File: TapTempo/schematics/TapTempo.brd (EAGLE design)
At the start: 60.6 x 50.5 mm, 40 parts, among them IC1 TL072D, IC2 MEGA168, IC3 LT1257S, Q301 BC846, Q701 BC846, Y1 16Mhz

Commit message: preliminary routing
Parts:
- removed C4: 100n, resistor:C0603
- removed IC3: LT1257S, linear-technology:SOIC8
- removed R2: 51K, resistor:R0603
- added BUTTON: (no value), SparkFun:1X04
- added C201: 100n, resistor:C0603
- added IC4: LM4041A12DBZ, texas:DBZ_R-PDSO-G3
- added R201: 100R, resistor:R0603
- added R202: 5K, resistor:R0603
- added R401, R402, R403, R404: 1K, resistor:R0603
- added U$1: MCP4921, Rebel:SOIC8
- moved IC1 32.7 mm to (36.2, 35.6), turned to 90 degrees
- moved R303 27.0 mm to (38.1, 19.7), turned to 270 degrees
- moved R301 22.2 mm to (36.8, 12.1), turned to 90 degrees
- moved R302 20.5 mm to (39.4, 12.1), turned to 90 degrees
- moved C3 20.4 mm to (14.6, 25.4), turned to 270 degrees
- moved Q301 18.9 mm to (38.1, 16.5), turned to 0 degrees
- moved R104 11.4 mm to (43.8, 19.1), turned to 180 degrees
- moved C1 9.55 mm to (24.8, 8.89), turned to 0 degrees
- moved R105 9.16 mm to (49.5, 27.9), turned to 0 degrees
- moved D2 8.89 mm to (12.1, 45.1)
- moved F2 8.26 mm to (20.3, 45.1)
- moved R101 7.18 mm to (49.5, 25.4)
- moved R102 7.18 mm to (49.5, 22.9), turned to 180 degrees
- moved R103 7.18 mm to (49.5, 30.5), turned to 0 degrees
- moved R1 5.85 mm to (28.6, 8.89), turned to 0 degrees
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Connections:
- removed net N$43: U$2.13, U$2.14
- removed net PWR_BUS: U$2.15, U$2.16
- removed net VCC: IC2.6
- new net LED+: BUTTON.3
- new net LED-: BUTTON.4
- new net N$13: R201.2, U$1.8
- new net N$19: IC1.6, R401.2, R403.1
- new net RAMP: IC1.5, R201.1, R402.1
- new net S1: BUTTON.1
- new net S2: BUTTON.2
- new net VREF: IC4.1, R202.2, R401.1, U$1.6
- net +12V: now also R202.1
- net +5V: now also C201.1, IC2.6, U$1.1; no longer C4.1, IC3.8
- net GND: now also C201.2, IC4.2, R402.2, U$1.7; no longer C4.2, IC3.5
- net N$7: now also R403.2, R404.1; no longer R2.1
- net N$8: now also R404.2; no longer R2.2
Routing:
- net +5V: track 0.00 -> 117.4 mm, vias 0 -> 2
- net +12V: track 0.00 -> 80.0 mm, vias 0 -> 2
- net N$1: track 0.00 -> 64.6 mm, vias 0 -> 1
- net GND: track 0.00 -> 63.2 mm, vias 0 -> 8
- net -12V: track 0.00 -> 46.8 mm
- net N$28: track 0.00 -> 38.6 mm, vias 0 -> 2
- net CMBOUT: track 0.00 -> 36.5 mm, vias 0 -> 2
- net VREF: track 0.00 -> 32.3 mm
- net DIVIN: track 0.00 -> 30.8 mm
- net RAMP: track 0.00 -> 29.9 mm
- net RX: track 0.00 -> 25.1 mm, vias 0 -> 1
- net N$3: track 0.00 -> 25.0 mm, vias 0 -> 2
- net N$2: track 0.00 -> 24.3 mm
- net TX: track 0.00 -> 24.1 mm, vias 0 -> 1
- net MODEA: track 0.00 -> 23.8 mm
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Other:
- board text added: "Rev 01"
- board text added: "Tap Tempo"
- board text removed: "Clock Delay"
- board text removed: "Rev 02"

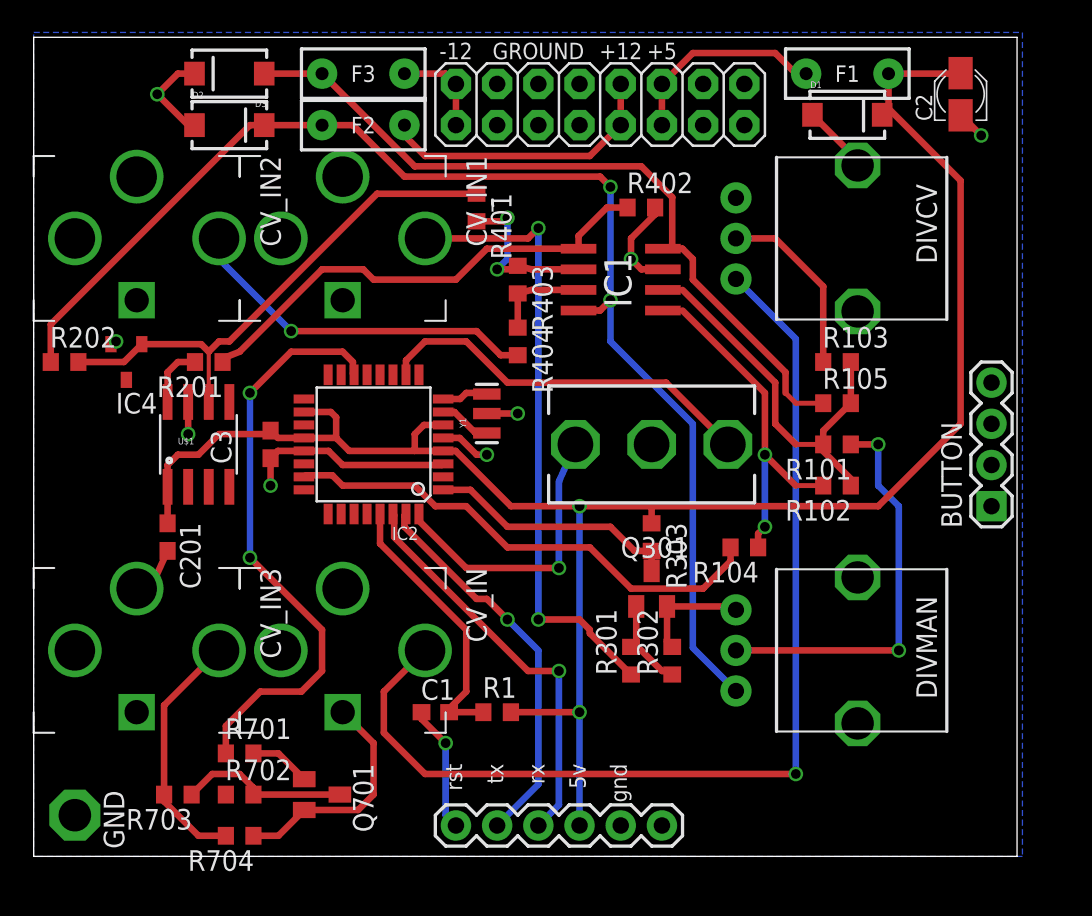
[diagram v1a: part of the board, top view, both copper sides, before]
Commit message: routed board with offsetting op amp as per MCP4921 datasheet
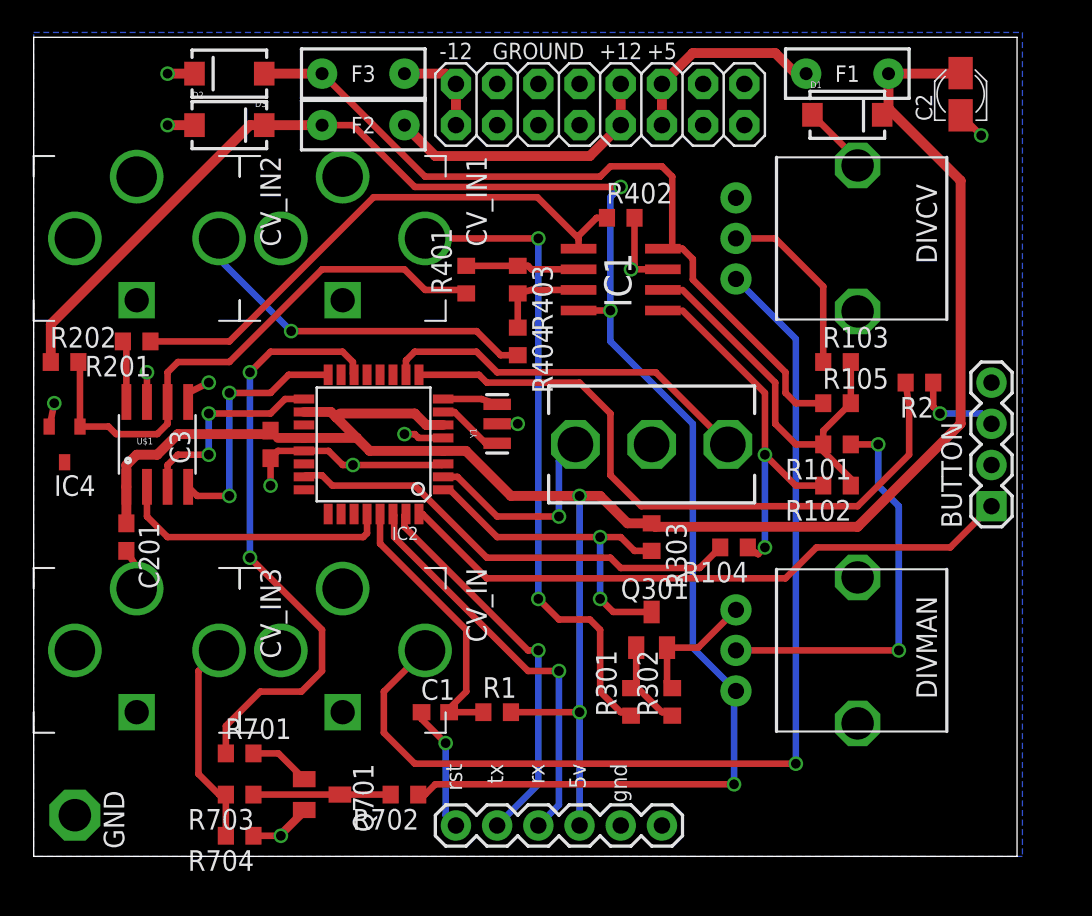
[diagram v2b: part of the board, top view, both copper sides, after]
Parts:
- added R2: 10K, resistor:R0603
- R403: value 1K -> 51K
- moved R702 10.2 mm to (22.9, 3.81), turned to 180 degrees
- moved IC4 6.35 mm to (1.91, 25.4)
- moved R201 4.62 mm to (6.35, 31.8)
- moved R401 4.49 mm to (26.7, 35.6), turned to 90 degrees
- moved R703 3.81 mm to (12.7, 3.81)
- moved C201 2.54 mm to (5.71, 19.7)
- moved Q301 2.54 mm to (38.1, 14.0)
- moved U$1 2.54 mm to (7.62, 25.4)
- moved R301 2.54 mm to (36.8, 9.53)
- moved R302 2.54 mm to (39.4, 9.53)
- moved R402 1.42 mm to (36.2, 39.4)
- moved Y1 0.90 mm to (28.6, 26.7)
- moved R104 0.63 mm to (43.2, 19.1)
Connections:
- net CLKIN renamed TRIGIN
- net CMBOUT renamed CLKOUT
- net DIVIN renamed SPEEDIN
- net MODEA renamed MODESW
- removed net LED-: BUTTON.4
- removed net N$17: IC2.28
- removed net RSTIN: IC2.32, S1.3
- removed net S1: BUTTON.1
- removed net S2: BUTTON.2
- removed net TRIGA: IC2.2
- new net CS: IC2.28, U$1.2
- new net SCK: IC2.17, U$1.3
- new net SDI: IC2.16, U$1.4
- new net STOPSW: IC2.2, S1.3
- new net SW1: BUTTON.1, IC2.32
- net +12V: now also R702.1
- net ALTA: now also R2.2
- net GND: now also BUTTON.2, BUTTON.4, U$1.5
- net LED+: now also R2.1
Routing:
- net ALTA: track 0.00 -> 41.6 mm
- net SW1: track 0.00 -> 38.8 mm
- net +12V: track 80.0 -> 106.2 mm, vias 2 -> 3
- net RSTIN: track 18.1 -> 0.00 mm, vias 1 -> 0
- net CS: track 0.00 -> 17.2 mm
- net SDI: track 0.00 -> 15.7 mm, vias 0 -> 2
- net STOPSW: track 0.00 -> 13.0 mm, vias 0 -> 1
- net SCK: track 0.00 -> 12.9 mm, vias 0 -> 2
- net GND: track 63.2 -> 54.3 mm, vias 8 -> 12
- net +5V: track 117.4 -> 125.1 mm
- net TRIGIN: track 15.6 -> 21.7 mm, vias 0 -> 2
- net LED+: track 0.00 -> 5.52 mm, vias 0 -> 1
- net RAMP: track 29.9 -> 34.1 mm
- net N$9: track 10.6 -> 7.01 mm, vias 2 -> 0
- net N$35: track 15.4 -> 12.9 mm
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
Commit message: updated routing
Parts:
- removed R201: 100R, resistor:R0603
- removed R404: 1K, resistor:R0603
- R202: value 5K -> 1K
- R401, R402: value 1K -> 120k
- R403: value 51K -> 100R
- moved R402 7.41 mm to (29.8, 35.6), turned to 270 degrees
- moved R703 4.02 mm to (8.89, 5.08)
- moved R704 4.02 mm to (8.89, 2.54)
- moved R403 3.81 mm to (29.8, 31.8)
- moved C201 3.59 mm to (3.17, 22.2), turned to 180 degrees
- moved C1 3.42 mm to (27.9, 10.2), turned to 180 degrees
- moved R1 1.42 mm to (27.9, 7.62)
- moved R702 1.27 mm to (22.9, 5.08)
- moved IC4 1.27 mm to (3.17, 25.4)
- moved R202 1.27 mm to (3.17, 30.5)
- moved R2 1.27 mm to (54.6, 30.5)
- moved R701 1.27 mm to (12.7, 5.08)
- moved R401 0.63 mm to (27.3, 35.6), turned to 270 degrees
- turned GND to 0 degrees
- renumbered CV_IN to SPEED, CV_IN1 to TRIG, CV_IN2 to RAMP, CV_IN3 to CLK, DIVCV to CV, DIVMAN to MANUAL
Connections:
- removed net N$13: R201.2, U$1.8
- net GND: now also R401.2, RAMP.P$1, RAMP.P$2, TRIG.P$4; no longer R402.2
- net N$7: now also R402.2, R403.1; no longer R403.2, R404.1
- net N$8: now also R403.2; no longer R404.2
- net N$9: now also R401.1, R402.1; no longer R401.2, R403.1
- net RAMP: now also U$1.8; no longer R201.1, R402.1
- net VREF: no longer R401.1
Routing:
- net VREF: track 34.7 -> 9.95 mm
- net GND: track 54.3 -> 43.8 mm, vias 12 -> 16
- net N$38: track 8.46 -> 13.4 mm
- net N$13: track 3.82 -> 0.00 mm
- net N$1: track 63.7 -> 60.1 mm
- net N$29: track 7.86 -> 11.3 mm
- net -12V: track 48.1 -> 45.1 mm
- net +12V: track 106.2 -> 103.5 mm, vias 3 -> 2
- net RAMP: track 34.1 -> 36.6 mm
- net +5V: track 125.1 -> 126.6 mm
- net N$35: track 12.9 -> 11.6 mm
- net LED+: track 5.52 -> 6.79 mm
- net ALTA: track 41.6 -> 42.8 mm
- net RX: track 25.1 -> 24.0 mm
- net N$39: track 17.0 -> 15.9 mm
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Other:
- board size 60.6 x 50.5 mm -> 60.6 x 50.3 mm

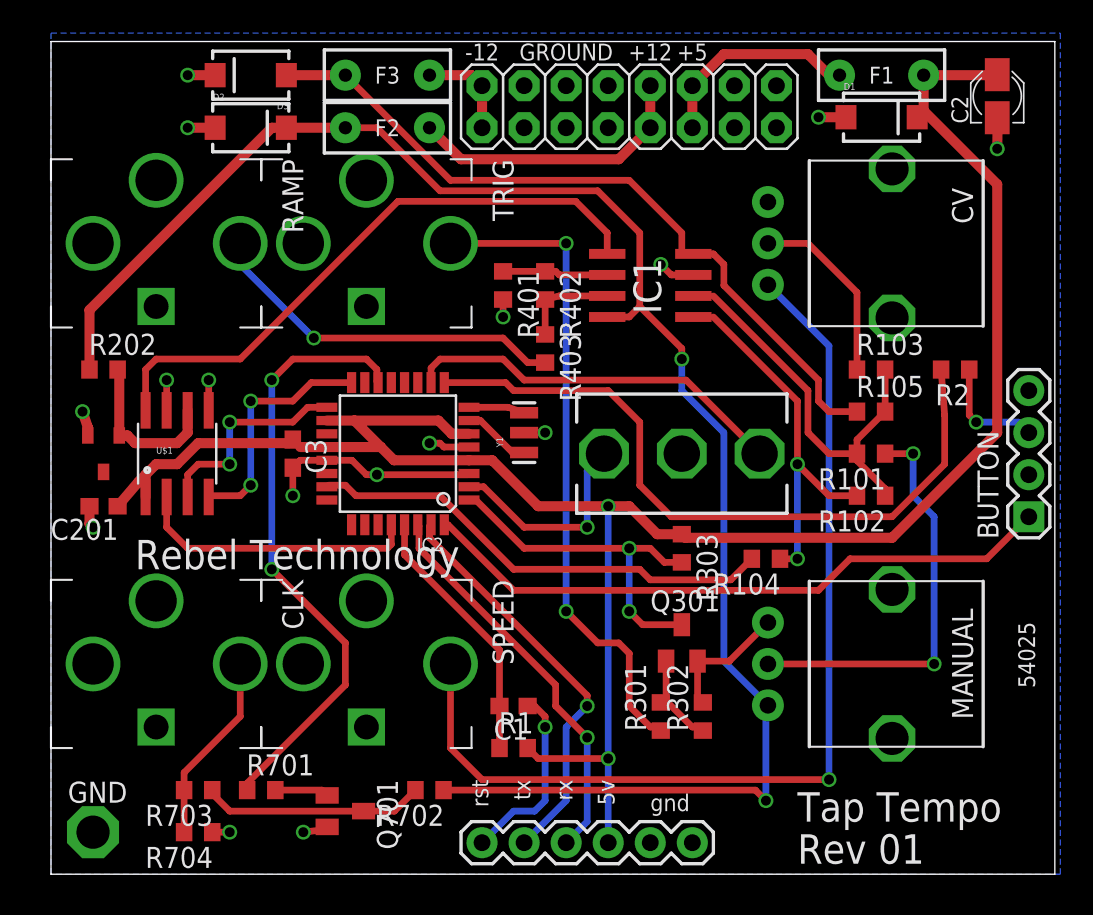
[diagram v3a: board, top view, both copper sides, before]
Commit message: re-aligned labels
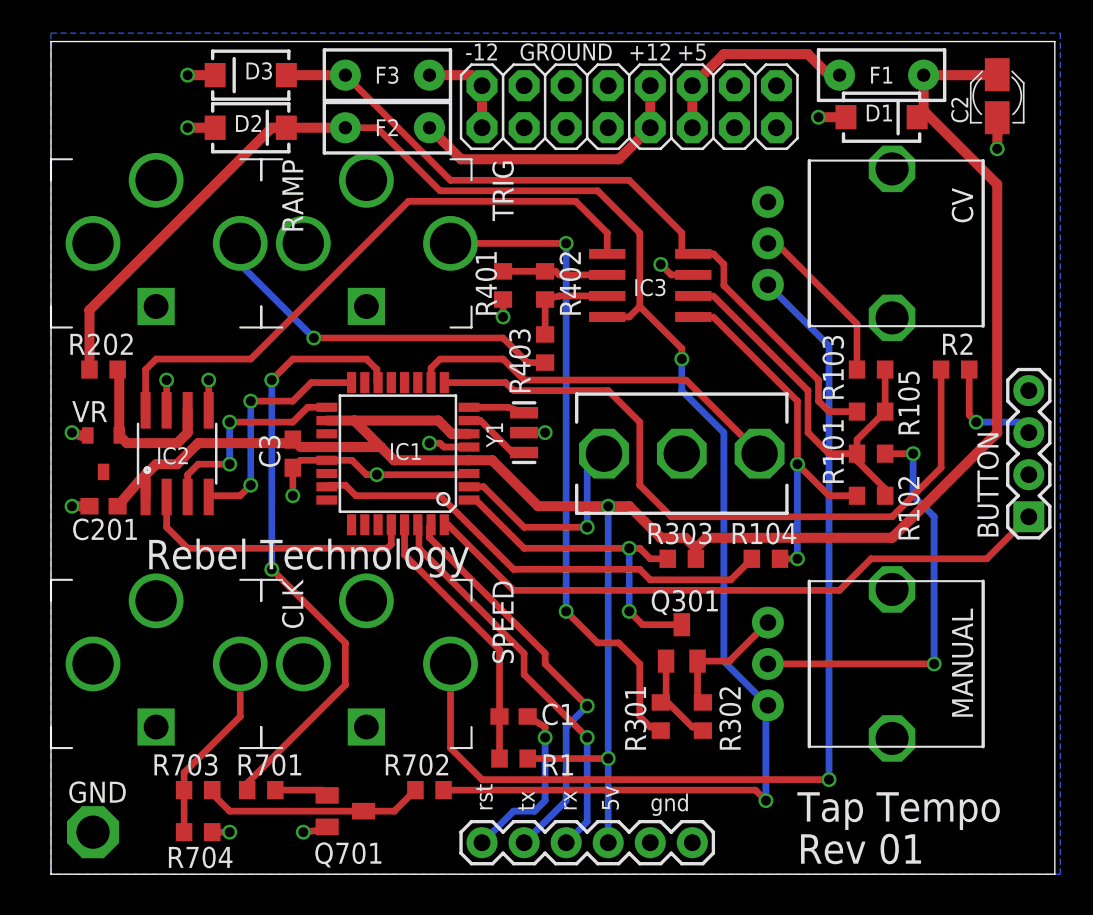
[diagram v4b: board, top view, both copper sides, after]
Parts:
- removed U$1: MCP4921, Rebel:SOIC8
- added IC3: TL072D, linear:SO08
- IC1: value TL072D -> MEGA168; device linear:SO08 -> atmel:TQFP32-08
- IC2: value MEGA168 -> MCP4921; device atmel:TQFP32-08 -> Rebel:SOIC8
- moved IC1 18.3 mm to (21.0, 25.4), turned to 180 degrees
- moved IC2 13.3 mm to (7.62, 25.4), turned to 0 degrees
- moved C1 0.63 mm to (27.9, 9.53)
- moved R1 0.63 mm to (27.9, 6.99)
- moved R303 0.63 mm to (38.1, 19.1), turned to 180 degrees
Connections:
- net +12V: now also IC3.8; no longer IC1.8
- net +5V: now also IC1.18, IC1.20, IC1.4, IC1.6, IC2.1; no longer IC2.18, IC2.20, IC2.4, IC2.6, U$1.1
- net -12V: now also IC3.4; no longer IC1.4
- net ALTA: now also IC1.9; no longer IC2.9
- net CLKOUT: now also IC1.14; no longer IC2.14
- net CS: now also IC1.28, IC2.2; no longer IC2.28, U$1.2
- net DELIN: now also IC1.24; no longer IC2.24
- net DELOUT: now also IC1.13; no longer IC2.13
- net DIVOUT: now also IC1.12; no longer IC2.12
- net GND: now also IC1.21, IC1.5, IC2.7, IC3.3; no longer IC2.21, IC2.3, U$1.5, U$1.7
- net MODEB: now also IC1.11; no longer IC2.11
- net MODESW: now also IC1.10; no longer IC2.10
- net N$14: now also IC1.25; no longer IC2.25
- net N$15: now also IC1.26; no longer IC2.26
- net N$16: now also IC1.27; no longer IC2.27
- net N$2: now also IC3.2; no longer IC1.2
- net N$20: now also IC1.7; no longer IC2.7
- net N$21: now also IC1.8; no longer IC2.8
- net N$39: now also IC1.29; no longer IC2.29
- net N$4: now also IC3.1; no longer IC1.1
- net N$7: now also IC3.7; no longer IC1.7
- net N$9: now also IC3.6; no longer IC1.6
- net RAMP: now also IC2.8, IC3.5; no longer IC1.5, U$1.8
- net RX: now also IC1.30; no longer IC2.30
- net SCK: now also IC1.17, IC2.3; no longer IC2.17, U$1.3
- net SDI: now also IC1.16, IC2.4; no longer IC2.16, U$1.4
- net SPEEDIN: now also IC1.23; no longer IC2.23
- net STOPSW: now also IC1.2; no longer IC2.2
- net SW1: now also IC1.32; no longer IC2.32
- net TRIGIN: now also IC1.1; no longer IC2.1
- net TX: now also IC1.31; no longer IC2.31
- net VREF: now also IC2.6; no longer U$1.6
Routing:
- net N$5: track 11.3 -> 10.2 mm
- net TRIGIN: track 21.7 -> 20.8 mm
- net +5V: track 126.6 -> 127.5 mm
- net N$29: track 11.3 -> 10.5 mm
- net GND: track 43.8 -> 43.2 mm
- net N$39: track 15.9 -> 16.5 mm
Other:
- board text added: "VR"
- board text removed: "54025"
